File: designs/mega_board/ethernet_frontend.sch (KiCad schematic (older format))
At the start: 53 parts

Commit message: Add comment on POE passthrough circuit
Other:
- note added: "This series resitor between \nPMOS gate and NMOS D is \nto keep PMOS Vgs at nomila \nvalues when the input POE \nvoltage is used at full range"
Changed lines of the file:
@@
 Wire Wire Line
 	2150 1000 1500 1000
+Text Notes 12600 7400 0    31   ~ 0
+This series resitor between \nPMOS gate and NMOS D is \nto keep PMOS Vgs at nomila \nvalues when the input POE \nvoltage is used at full range
 $EndSCHEMATC

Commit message: Enumerate components as is in eagle design.
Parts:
- removed Q?: BSS138-7-F, symbol Device:Q_NMOS_DSG
- removed Q?: Si4435DDY-T1, symbol Device:Q_PMOS_DSG
- added Q11: BSS138-7-F, LibreRouter_MegaBoard:SOT-23, symbol nmosfet:NMOSFET
- added Q9: Si4435DDY-T1, LibreRouter_MegaBoard:SI4435, symbol p-mosfet_so8:P-MOSFET_SO8
- C10, C11, C137, C33, C34, C35, C37, C5: renamed from C?; footprint (none) -> LibreRouter_MegaBoard:C0402
- C40, C41, C49: renamed from C?; footprint (none) -> LibreRouter_MegaBoard:C1206
- D10, D11, D3, D4, D6, D7, D8, D9: renamed from D?; footprint (none) -> LibreRouter_MegaBoard:SOD−323
- P1, P2, P3, P4, P5, P6, P7, P8: renamed from U?; footprint (none) -> LibreRouter_MegaBoard:GDT-LT-B3D090L
- R1, R29, R3, R30, R31, R32, R4, R44, R5, R57, R6: renamed from R?; footprint (none) -> LibreRouter_MegaBoard:R0402
- R2: renamed from R?; value 75 -> 75,NL; footprint (none) -> LibreRouter_MegaBoard:R0402
- R22, R25, R8: renamed from R?; footprint (none) -> LibreRouter_MegaBoard:R1206
- R33: renamed from R?; value 0 -> 0R 1/10W; footprint (none) -> LibreRouter_MegaBoard:R0603
- T1: renamed from U?; footprint (none) -> LibreRouter_MegaBoard:QT48103
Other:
- moved on the sheet: R3, R32, R44

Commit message: Add capacitor definito to BOM
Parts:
- C10, C11, C137, C33, C34, C35, C37, C5: Manufacturer (none) -> Murata Electronics; Manufacturer PN (none) -> GCM155R71A104KA55D; Supplier (none) -> DigiKey; Supplier PN (none) -> 490-16434-6-ND
- C40, C41, C49: Manufacturer (none) -> Murata Electronics; Manufacturer PN (none) -> GCJ31CR73A103KXJ3L; Supplier (none) -> DigiKey; Supplier PN (none) -> 490-16694-6-ND
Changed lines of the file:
@@
 F 2 "LibreRouter_MegaBoard:C0402" H 2588 2700 50  0001 C CNN
 F 3 "~" H 2550 2850 50  0001 C CNN
+F 4 "Murata Electronics" H 2550 2850 50  0001 C CNN "Manufacturer"
+F 5 "GCM155R71A104KA55D" H 2550 2850 50  0001 C CNN "Manufacturer PN"
+F 6 "DigiKey" H 2550 2850 50  0001 C CNN "Supplier"
+F 7 "490-16434-6-ND" H 2550 2850 50  0001 C CNN "Supplier PN"
 	1    2550 2850
 	1    0    0    -1
@@
 F 2 "LibreRouter_MegaBoard:C0402" H 2588 4500 50  0001 C CNN
 F 3 "~" H 2550 4650 50  0001 C CNN
+F 4 "Murata Electronics" H 2550 4650 50  0001 C CNN "Manufacturer"
+F 5 "GCM155R71A104KA55D" H 2550 4650 50  0001 C CNN "Manufacturer PN"
+F 6 "DigiKey" H 2550 4650 50  0001 C CNN "Supplier"
+F 7 "490-16434-6-ND" H 2550 4650 50  0001 C CNN "Supplier PN"
 	1    2550 4650
 	1    0    0    -1
@@
 F 2 "LibreRouter_MegaBoard:C0402" H 2588 6200 50  0001 C CNN
 F 3 "~" H 2550 6350 50  0001 C CNN
+F 4 "Murata Electronics" H 2550 6350 50  0001 C CNN "Manufacturer"
+F 5 "GCM155R71A104KA55D" H 2550 6350 50  0001 C CNN "Manufacturer PN"
+F 6 "DigiKey" H 2550 6350 50  0001 C CNN "Supplier"
+F 7 "490-16434-6-ND" H 2550 6350 50  0001 C CNN "Supplier PN"
 	1    2550 6350
 	1    0    0    -1
@@
 F 2 "LibreRouter_MegaBoard:C0402" H 2588 8000 50  0001 C CNN
 F 3 "~" H 2550 8150 50  0001 C CNN
+F 4 "Murata Electronics" H 2550 8150 50  0001 C CNN "Manufacturer"
+F 5 "GCM155R71A104KA55D" H 2550 8150 50  0001 C CNN "Manufacturer PN"
+F 6 "DigiKey" H 2550 8150 50  0001 C CNN "Supplier"
+F 7 "490-16434-6-ND" H 2550 8150 50  0001 C CNN "Supplier PN"
 	1    2550 8150
 	1    0    0    -1
@@
 F 2 "LibreRouter_MegaBoard:C0402" H 8238 2700 50  0001 C CNN
 F 3 "~" H 8200 2850 50  0001 C CNN
+F 4 "Murata Electronics" H 8200 2850 50  0001 C CNN "Manufacturer"
+F 5 "GCM155R71A104KA55D" H 8200 2850 50  0001 C CNN "Manufacturer PN"
+F 6 "DigiKey" H 8200 2850 50  0001 C CNN "Supplier"
+F 7 "490-16434-6-ND" H 8200 2850 50  0001 C CNN "Supplier PN"
 	1    8200 2850
 	1    0    0    -1
@@
 F 2 "LibreRouter_MegaBoard:C0402" H 8238 4500 50  0001 C CNN
 F 3 "~" H 8200 4650 50  0001 C CNN
+F 4 "Murata Electronics" H 8200 4650 50  0001 C CNN "Manufacturer"
+F 5 "GCM155R71A104KA55D" H 8200 4650 50  0001 C CNN "Manufacturer PN"
+F 6 "DigiKey" H 8200 4650 50  0001 C CNN "Supplier"
+F 7 "490-16434-6-ND" H 8200 4650 50  0001 C CNN "Supplier PN"
 	1    8200 4650
 	1    0    0    -1
@@
 F 2 "LibreRouter_MegaBoard:C0402" H 8238 6200 50  0001 C CNN
 F 3 "~" H 8200 6350 50  0001 C CNN
+F 4 "Murata Electronics" H 8200 6350 50  0001 C CNN "Manufacturer"
+F 5 "GCM155R71A104KA55D" H 8200 6350 50  0001 C CNN "Manufacturer PN"
+F 6 "DigiKey" H 8200 6350 50  0001 C CNN "Supplier"
+F 7 "490-16434-6-ND" H 8200 6350 50  0001 C CNN "Supplier PN"
 	1    8200 6350
 	1    0    0    -1
@@
 F 2 "LibreRouter_MegaBoard:C0402" H 8238 8000 50  0001 C CNN
 F 3 "~" H 8200 8150 50  0001 C CNN
+F 4 "Murata Electronics" H 8200 8150 50  0001 C CNN "Manufacturer"
+F 5 "GCM155R71A104KA55D" H 8200 8150 50  0001 C CNN "Manufacturer PN"
+F 6 "DigiKey" H 8200 8150 50  0001 C CNN "Supplier"
+F 7 "490-16434-6-ND" H 8200 8150 50  0001 C CNN "Supplier PN"
 	1    8200 8150
 	1    0    0    -1
@@
 F 2 "LibreRouter_MegaBoard:C1206" H 15088 2850 50  0001 C CNN
 F 3 "~" H 15050 3000 50  0001 C CNN
+F 4 "DigiKey" H 15050 3000 50  0001 C CNN "Supplier"
+F 5 "Murata Electronics" H 15050 3000 50  0001 C CNN "Manufacturer"
+F 6 "GCJ31CR73A103KXJ3L" H 15050 3000 50  0001 C CNN "Manufacturer PN"
+F 7 "490-16694-6-ND" H 15050 3000 50  0001 C CNN "Supplier PN"
 	1    15050 3000
 	1    0    0    -1
@@
 F 2 "LibreRouter_MegaBoard:C1206" H 14788 7000 50  0001 C CNN
 F 3 "~" H 14750 7150 50  0001 C CNN
+F 4 "DigiKey" H 14750 7150 50  0001 C CNN "Supplier"
+F 5 "Murata Electronics" H 14750 7150 50  0001 C CNN "Manufacturer"
+F 6 "GCJ31CR73A103KXJ3L" H 14750 7150 50  0001 C CNN "Manufacturer PN"
+F 7 "490-16694-6-ND" H 14750 7150 50  0001 C CNN "Supplier PN"
 	1    14750 7150
 	1    0    0    -1
@@
 F 2 "LibreRouter_MegaBoard:C1206" H 13238 4650 50  0001 C CNN
 F 3 "~" H 13200 4800 50  0001 C CNN
+F 4 "DigiKey" H 13200 4800 50  0001 C CNN "Supplier"
+F 5 "Murata Electronics" H 13200 4800 50  0001 C CNN "Manufacturer"
+F 6 "GCJ31CR73A103KXJ3L" H 13200 4800 50  0001 C CNN "Manufacturer PN"
+F 7 "490-16694-6-ND" H 13200 4800 50  0001 C CNN "Supplier PN"
 	1    13200 4800
 	1    0    0    -1

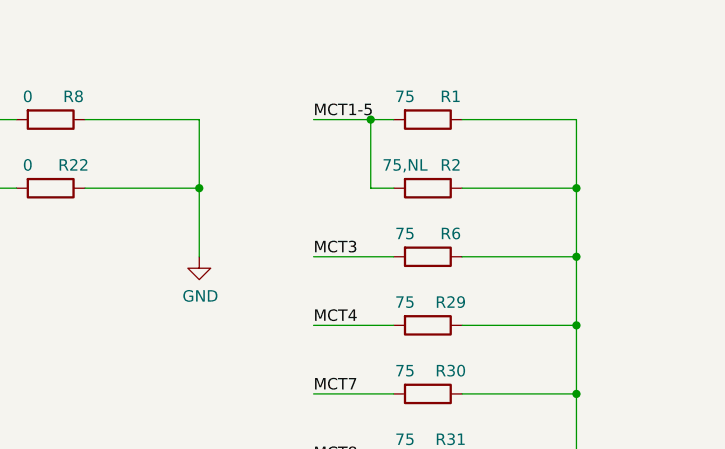
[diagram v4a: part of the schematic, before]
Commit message: Add DNP column. Add some connectors BOM definition.
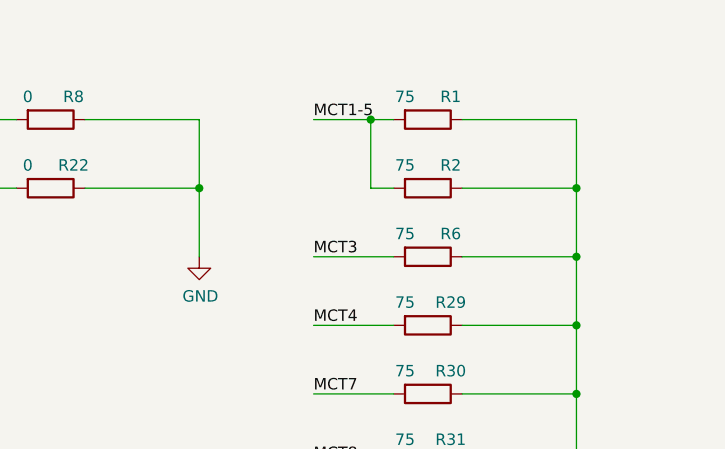
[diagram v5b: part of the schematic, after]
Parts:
- R2: value 75,NL -> 75; DNP (none) -> DNP
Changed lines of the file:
@@
 P 14400 1650
 F 0 "R2" V 14300 1750 50  0000 C CNN
-F 1 "75,NL" V 14300 1550 50  0000 C CNN
+F 1 "75" V 14300 1550 50  0000 C CNN
 F 2 "LibreRouter_MegaBoard:R0402" V 14330 1650 50  0001 C CNN
 F 3 "~" H 14400 1650 50  0001 C CNN
+F 4 "DNP" H 14400 1650 50  0001 C CNN "DNP"
 	1    14400 1650
 	0    1    1    0

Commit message: Add BOM definition for almost all diodes
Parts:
- D10, D11, D3, D4, D6, D7, D8, D9: Supplier (none) -> DigiKey
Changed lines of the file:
@@
 F 2 "LibreRouter_MegaBoard:SOD−323" H 1700 2400 50  0001 C CNN
 F 3 "~" H 1700 2400 50  0001 C CNN
+F 4 "DigiKey" H 1700 2400 50  0001 C CNN "Supplier"
 	1    1700 2400
 	0    1    1    0
@@
 F 2 "LibreRouter_MegaBoard:SOD−323" H 1700 4200 50  0001 C CNN
 F 3 "~" H 1700 4200 50  0001 C CNN
+F 4 "DigiKey" H 1700 4200 50  0001 C CNN "Supplier"
 	1    1700 4200
 	0    1    1    0
@@
 F 2 "LibreRouter_MegaBoard:SOD−323" H 1700 5900 50  0001 C CNN
 F 3 "~" H 1700 5900 50  0001 C CNN
+F 4 "DigiKey" H 1700 5900 50  0001 C CNN "Supplier"
 	1    1700 5900
 	0    1    1    0
@@
 F 2 "LibreRouter_MegaBoard:SOD−323" H 1700 7700 50  0001 C CNN
 F 3 "~" H 1700 7700 50  0001 C CNN
+F 4 "DigiKey" H 1700 7700 50  0001 C CNN "Supplier"
 	1    1700 7700
 	0    1    1    0
@@
 F 2 "LibreRouter_MegaBoard:SOD−323" H 7350 2400 50  0001 C CNN
 F 3 "~" H 7350 2400 50  0001 C CNN
+F 4 "DigiKey" H 7350 2400 50  0001 C CNN "Supplier"
 	1    7350 2400
 	0    1    1    0
@@
 F 2 "LibreRouter_MegaBoard:SOD−323" H 7350 4200 50  0001 C CNN
 F 3 "~" H 7350 4200 50  0001 C CNN
+F 4 "DigiKey" H 7350 4200 50  0001 C CNN "Supplier"
 	1    7350 4200
 	0    1    1    0
@@
 F 2 "LibreRouter_MegaBoard:SOD−323" H 7350 5900 50  0001 C CNN
 F 3 "~" H 7350 5900 50  0001 C CNN
+F 4 "DigiKey" H 7350 5900 50  0001 C CNN "Supplier"
 	1    7350 5900
 	0    1    1    0
@@
 F 2 "LibreRouter_MegaBoard:SOD−323" H 7350 7700 50  0001 C CNN
 F 3 "~" H 7350 7700 50  0001 C CNN
+F 4 "DigiKey" H 7350 7700 50  0001 C CNN "Supplier"
 	1    7350 7700
 	0    1    1    0

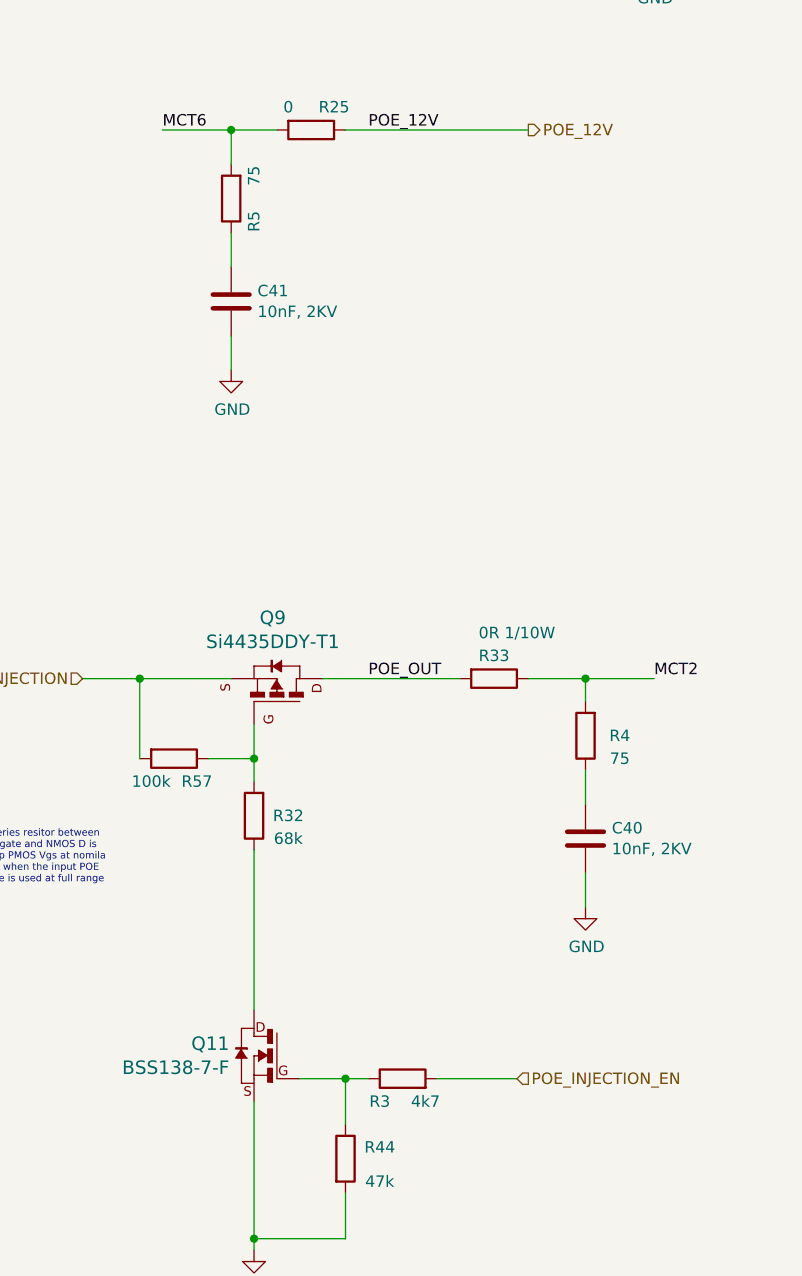
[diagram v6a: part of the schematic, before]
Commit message: Add BOM definition to all resistors
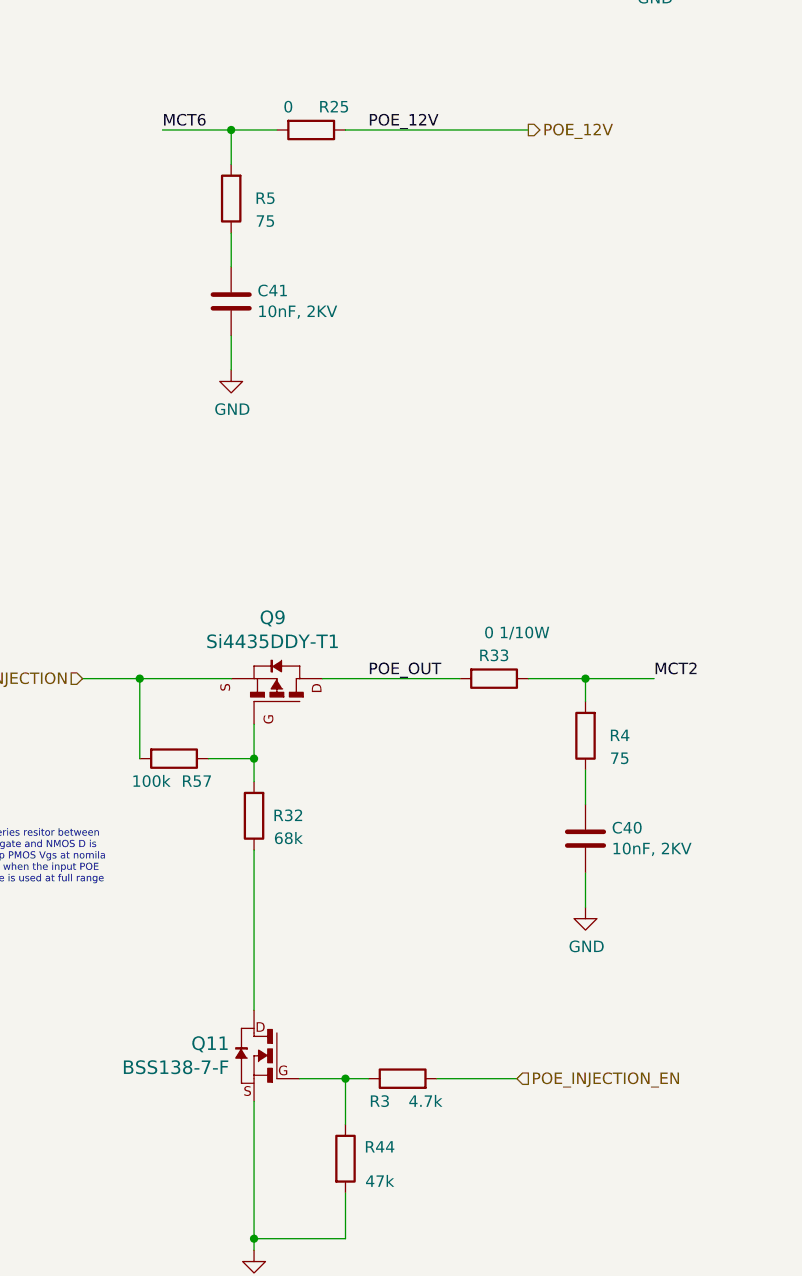
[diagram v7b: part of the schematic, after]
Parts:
- R1, R2, R29, R30, R31, R4, R5, R6: Manufacturer (none) -> Panasonic Electronic Components; Manufacturer PN (none) -> ERJ-2BWFR075X; Supplier (none) -> DigiKey; Supplier PN (none) -> P.075ATDKR-ND
- R22, R25, R8: Manufacturer (none) -> Panasonic Electronic Components; Manufacturer PN (none) -> ERJ-8GEY0R00V; Supplier (none) -> DigiKey; Supplier PN (none) -> P0.0EDKR-ND
- R3: value 4k7 -> 4.7k; Manufacturer (none) -> Panasonic Electronic Components; Manufacturer PN (none) -> ERJ-2GEJ472X; Supplier (none) -> DigiKey; Supplier PN (none) -> P4.7KJDKR-ND
- R32: Manufacturer (none) -> Panasonic Electronic Components; Manufacturer PN (none) -> ERJ-PA2F6802X; Supplier (none) -> DigiKey; Supplier PN (none) -> P17235DKR-ND
- R33: value 0R 1/10W -> 0 1/10W; Manufacturer (none) -> Panasonic Electronic Components; Manufacturer PN (none) -> ERJ-3GEY0R00V; Supplier (none) -> DigiKey; Supplier PN (none) -> P0.0GDKR-ND
- R44: Manufacturer (none) -> Panasonic Electronic Components; Manufacturer PN (none) -> ERJ-PA2F4702X; Supplier (none) -> DigiKey; Supplier PN (none) -> P17234DKR-ND
- R57: Manufacturer (none) -> Panasonic Electronic Components; Manufacturer PN (none) -> ERJ-PA2F1003X; Supplier (none) -> DigiKey; Supplier PN (none) -> P17236DKR-ND
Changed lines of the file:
@@
 F 3 "~" H 14400 1650 50  0001 C CNN
 F 4 "DNP" H 14400 1650 50  0001 C CNN "DNP"
+F 5 "Panasonic Electronic Components" H 14400 1650 50  0001 C CNN "Manufacturer"
+F 6 "ERJ-2BWFR075X" H 14400 1650 50  0001 C CNN "Manufacturer PN"
+F 7 "DigiKey" H 14400 1650 50  0001 C CNN "Supplier"
+F 8 "P.075ATDKR-ND" H 14400 1650 50  0001 C CNN "Supplier PN"
 	1    14400 1650
 	0    1    1    0
@@
 F 2 "LibreRouter_MegaBoard:R0402" V 14330 1950 50  0001 C CNN
 F 3 "~" H 14400 1950 50  0001 C CNN
+F 4 "Panasonic Electronic Components" H 14400 1950 50  0001 C CNN "Manufacturer"
+F 5 "ERJ-2BWFR075X" H 14400 1950 50  0001 C CNN "Manufacturer PN"
+F 6 "DigiKey" H 14400 1950 50  0001 C CNN "Supplier"
+F 7 "P.075ATDKR-ND" H 14400 1950 50  0001 C CNN "Supplier PN"
 	1    14400 1950
 	0    1    1    0
@@
 F 2 "LibreRouter_MegaBoard:R0402" V 14330 2250 50  0001 C CNN
 F 3 "~" H 14400 2250 50  0001 C CNN
+F 4 "Panasonic Electronic Components" H 14400 2250 50  0001 C CNN "Manufacturer"
+F 5 "ERJ-2BWFR075X" H 14400 2250 50  0001 C CNN "Manufacturer PN"
+F 6 "DigiKey" H 14400 2250 50  0001 C CNN "Supplier"
+F 7 "P.075ATDKR-ND" H 14400 2250 50  0001 C CNN "Supplier PN"
 	1    14400 2250
 	0    1    1    0
@@
 F 2 "LibreRouter_MegaBoard:R0402" V 14330 2550 50  0001 C CNN
 F 3 "~" H 14400 2550 50  0001 C CNN
+F 4 "Panasonic Electronic Components" H 14400 2550 50  0001 C CNN "Manufacturer"
+F 5 "ERJ-2BWFR075X" H 14400 2550 50  0001 C CNN "Manufacturer PN"
+F 6 "DigiKey" H 14400 2550 50  0001 C CNN "Supplier"
+F 7 "P.075ATDKR-ND" H 14400 2550 50  0001 C CNN "Supplier PN"
 	1    14400 2550
 	0    1    1    0
@@
 F 2 "LibreRouter_MegaBoard:R0402" V 14330 2850 50  0001 C CNN
 F 3 "~" H 14400 2850 50  0001 C CNN
+F 4 "Panasonic Electronic Components" H 14400 2850 50  0001 C CNN "Manufacturer"
+F 5 "ERJ-2BWFR075X" H 14400 2850 50  0001 C CNN "Manufacturer PN"
+F 6 "DigiKey" H 14400 2850 50  0001 C CNN "Supplier"
+F 7 "P.075ATDKR-ND" H 14400 2850 50  0001 C CNN "Supplier PN"
 	1    14400 2850
 	0    1    1    0
@@
 F 2 "LibreRouter_MegaBoard:R0402" V 14330 1350 50  0001 C CNN
 F 3 "~" H 14400 1350 50  0001 C CNN
+F 4 "Panasonic Electronic Components" H 14400 1350 50  0001 C CNN "Manufacturer"
+F 5 "ERJ-2BWFR075X" H 14400 1350 50  0001 C CNN "Manufacturer PN"
+F 6 "DigiKey" H 14400 1350 50  0001 C CNN "Supplier"
+F 7 "P.075ATDKR-ND" H 14400 1350 50  0001 C CNN "Supplier PN"
 	1    14400 1350
 	0    1    1    0
@@
 U 1 1 5D6301C2
 P 13200 4350
-F 0 "R5" V 13100 4450 50  0000 C CNN
-F 1 "75" V 13100 4250 50  0000 C CNN
+F 0 "R5" H 13050 4350 50  0000 C CNN
+F 1 "75" H 13050 4450 50  0000 C CNN
 F 2 "LibreRouter_MegaBoard:R0402" V 13130 4350 50  0001 C CNN
 F 3 "~" H 13200 4350 50  0001 C CNN
+F 4 "Panasonic Electronic Components" H 13200 4350 50  0001 C CNN "Manufacturer"
+F 5 "ERJ-2BWFR075X" H 13200 4350 50  0001 C CNN "Manufacturer PN"
+F 6 "DigiKey" H 13200 4350 50  0001 C CNN "Supplier"
+F 7 "P.075ATDKR-ND" H 13200 4350 50  0001 C CNN "Supplier PN"
 	1    13200 4350
 	-1   0    0    1
@@
 F 2 "LibreRouter_MegaBoard:R0402" V 14680 6700 50  0001 C CNN
 F 3 "~" H 14750 6700 50  0001 C CNN
+F 4 "Panasonic Electronic Components" H 14750 6700 50  0001 C CNN "Manufacturer"
+F 5 "ERJ-2BWFR075X" H 14750 6700 50  0001 C CNN "Manufacturer PN"
+F 6 "DigiKey" H 14750 6700 50  0001 C CNN "Supplier"
+F 7 "P.075ATDKR-ND" H 14750 6700 50  0001 C CNN "Supplier PN"
 	1    14750 6700
 	-1   0    0    1
@@
 F 2 "LibreRouter_MegaBoard:R1206" V 12680 1650 50  0001 C CNN
 F 3 "~" H 12750 1650 50  0001 C CNN
+F 4 "Panasonic Electronic Components" H 12750 1650 50  0001 C CNN "Manufacturer"
+F 5 "DigiKey" H 12750 1650 50  0001 C CNN "Supplier"
+F 6 "ERJ-8GEY0R00V" H 12750 1650 50  0001 C CNN "Manufacturer PN"
+F 7 "P0.0EDKR-ND" H 12750 1650 50  0001 C CNN "Supplier PN"
 	1    12750 1650
 	0    1    1    0
@@
 F 2 "LibreRouter_MegaBoard:R1206" V 12680 1350 50  0001 C CNN
 F 3 "~" H 12750 1350 50  0001 C CNN
+F 4 "Panasonic Electronic Components" H 12750 1350 50  0001 C CNN "Manufacturer"
+F 5 "DigiKey" H 12750 1350 50  0001 C CNN "Supplier"
+F 6 "ERJ-8GEY0R00V" H 12750 1350 50  0001 C CNN "Manufacturer PN"
+F 7 "P0.0EDKR-ND" H 12750 1350 50  0001 C CNN "Supplier PN"
 	1    12750 1350
 	0    1    1    0
@@
 F 2 "LibreRouter_MegaBoard:R1206" V 13480 4050 50  0001 C CNN
 F 3 "~" H 13550 4050 50  0001 C CNN
+F 4 "Panasonic Electronic Components" H 13550 4050 50  0001 C CNN "Manufacturer"
+F 5 "DigiKey" H 13550 4050 50  0001 C CNN "Supplier"
+F 6 "ERJ-8GEY0R00V" H 13550 4050 50  0001 C CNN "Manufacturer PN"
+F 7 "P0.0EDKR-ND" H 13550 4050 50  0001 C CNN "Supplier PN"
 	1    13550 4050
 	0    1    1    0
@@
 P 14350 6450
 F 0 "R33" V 14250 6450 50  0000 C CNN
-F 1 "0R 1/10W" V 14150 6550 50  0000 C CNN
+F 1 "0 1/10W" V 14150 6550 50  0000 C CNN
 F 2 "LibreRouter_MegaBoard:R0603" V 14280 6450 50  0001 C CNN
 F 3 "~" H 14350 6450 50  0001 C CNN
+F 4 "Panasonic Electronic Components" H 14350 6450 50  0001 C CNN "Manufacturer"
+F 5 "DigiKey" H 14350 6450 50  0001 C CNN "Supplier"
+F 6 "ERJ-3GEY0R00V" H 14350 6450 50  0001 C CNN "Manufacturer PN"
+F 7 "P0.0GDKR-ND" H 14350 6450 50  0001 C CNN "Supplier PN"
 	1    14350 6450
 	0    1    1    0
@@
 F 2 "LibreRouter_MegaBoard:R0402" V 13230 7050 50  0001 C CNN
 F 3 "~" H 13300 7050 50  0001 C CNN
+F 4 "Panasonic Electronic Components" H 13300 7050 50  0001 C CNN "Manufacturer"
+F 5 "ERJ-PA2F6802X" H 13300 7050 50  0001 C CNN "Manufacturer PN"
+F 6 "DigiKey" H 13300 7050 50  0001 C CNN "Supplier"
+F 7 "P17235DKR-ND" H 13300 7050 50  0001 C CNN "Supplier PN"
 	1    13300 7050
 	-1   0    0    1
@@
 F 2 "LibreRouter_MegaBoard:R0402" V 12880 6800 50  0001 C CNN
 F 3 "~" H 12950 6800 50  0001 C CNN
+F 4 "Panasonic Electronic Components" H 12950 6800 50  0001 C CNN "Manufacturer"
+F 5 "ERJ-PA2F1003X" H 12950 6800 50  0001 C CNN "Manufacturer PN"
+F 6 "DigiKey" H 12950 6800 50  0001 C CNN "Supplier"
+F 7 "P17236DKR-ND" H 12950 6800 50  0001 C CNN "Supplier PN"
 	1    12950 6800
 	0    1    1    0
@@
 P 13950 8200
 F 0 "R3" V 13850 8300 50  0000 C CNN
-F 1 "4k7" V 13850 8100 50  0000 C CNN
+F 1 "4.7k" V 13850 8100 50  0000 C CNN
 F 2 "LibreRouter_MegaBoard:R0402" V 13880 8200 50  0001 C CNN
 F 3 "~" H 13950 8200 50  0001 C CNN
+F 4 "Panasonic Electronic Components" H 13950 8200 50  0001 C CNN "Manufacturer"
+F 5 "ERJ-2GEJ472X" H 13950 8200 50  0001 C CNN "Manufacturer PN"
+F 6 "DigiKey" H 13950 8200 50  0001 C CNN "Supplier"
+F 7 "P4.7KJDKR-ND" H 13950 8200 50  0001 C CNN "Supplier PN"
 	1    13950 8200
 	0    -1   -1   0
@@
 F 2 "LibreRouter_MegaBoard:R0402" V 13630 8550 50  0001 C CNN
 F 3 "~" H 13700 8550 50  0001 C CNN
+F 4 "Panasonic Electronic Components" H 13700 8550 50  0001 C CNN "Manufacturer"
+F 5 "ERJ-PA2F4702X" H 13700 8550 50  0001 C CNN "Manufacturer PN"
+F 6 "DigiKey" H 13700 8550 50  0001 C CNN "Supplier"
+F 7 "P17234DKR-ND" H 13700 8550 50  0001 C CNN "Supplier PN"
 	1    13700 8550
 	1    0    0    -1
